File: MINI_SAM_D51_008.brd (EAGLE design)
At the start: 25.4 x 40.4 mm, 32 parts, among them IC2 PRTR5V0U2X, IC4 ATSAMD51G_TQFN48, J1 MOLEX_47346-100147346, J2 CORTEX_DEBUG_PTH, SW1 KMS233GLFG, SW2 KMS233GLFG, U1 GD25x16

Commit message: Adjust VREG
Tried a new layout with VREG aligned to torso.
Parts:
- moved C11 0.48 mm to (20.9, 17.3), turned to 7.9 degrees
- moved VREG 0.11 mm to (20.6, 20.1), turned to 187.9 degrees
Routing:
- net VIN: track 15.6 -> 9.93 mm
- net !RESET: track 17.3 -> 16.5 mm
- net VDD: track 87.5 -> 86.8 mm
- net GND: vias 22 -> 20
- added copper zone on layer 1, net VIN

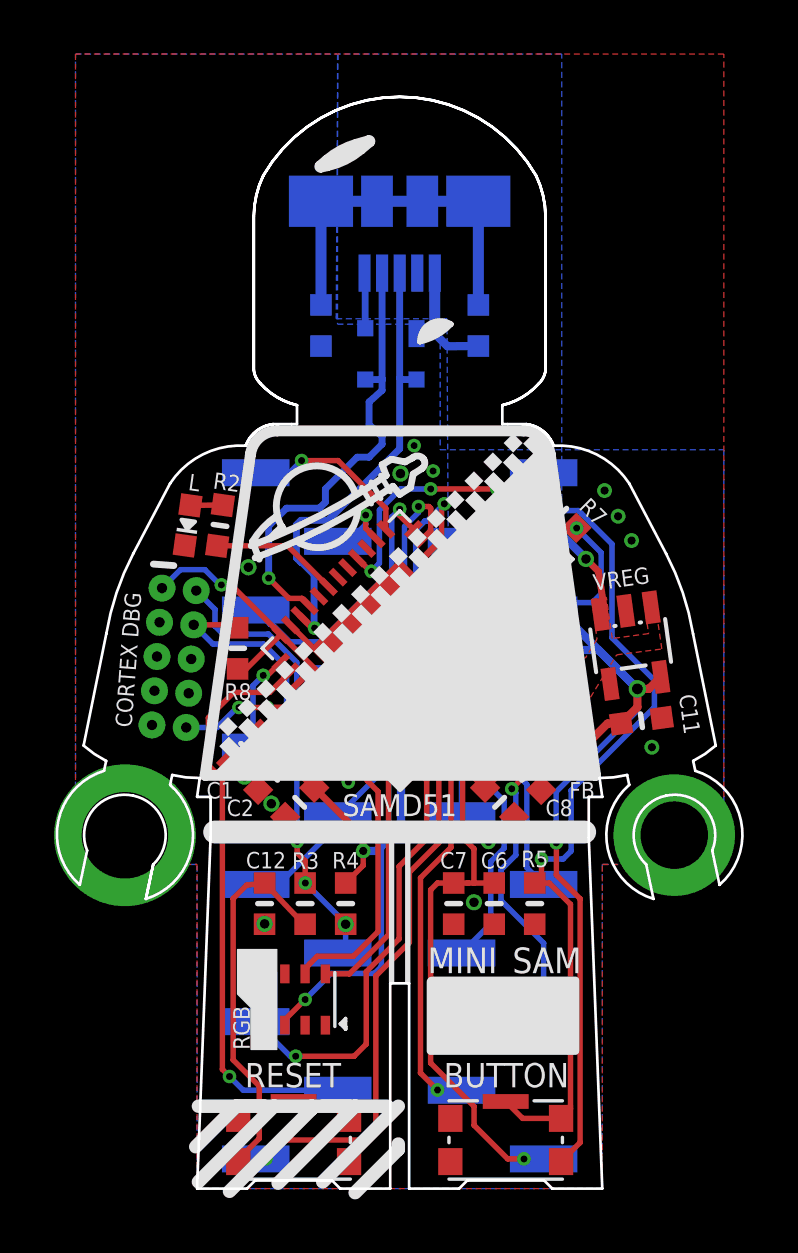
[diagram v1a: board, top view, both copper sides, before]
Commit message: Minor Mods
Modified layout slightly.  Will require a new sold paste template.
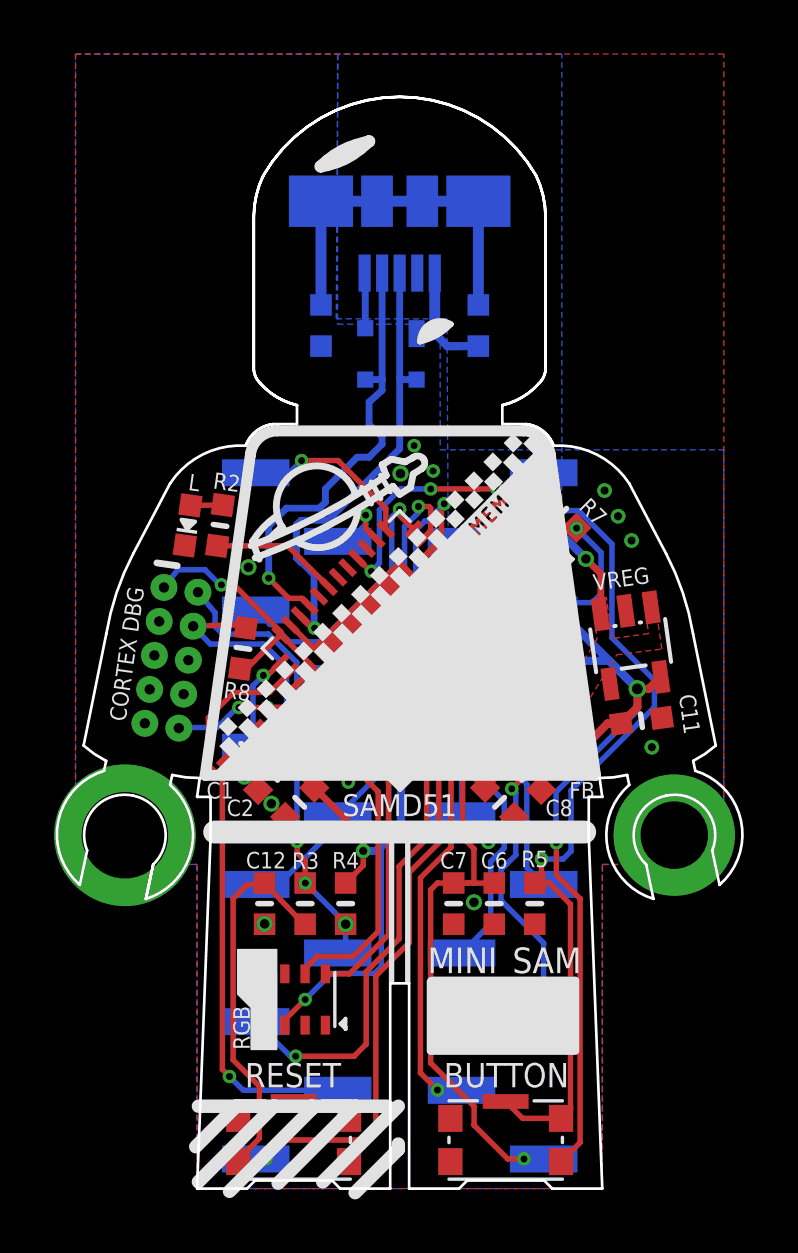
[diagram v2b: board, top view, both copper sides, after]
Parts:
- moved R8 0.20 mm to (6.20, 20.0), turned to 262 degrees
- moved C10 0.20 mm to (17.8, 20.0), turned to 278 degrees
- moved J2 0.10 mm to (3.55, 19.6), turned to 262 degrees
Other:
- board text removed: "MEM"
